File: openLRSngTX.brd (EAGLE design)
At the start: 50 x 40.2 mm, 28 parts, among them IC1 RFM23BPSMD, J1 AVR_SPI_PRG_6PTH, Q1 MMBT2222, U1 ATMEGA328P, X1 BU-SMA-V, Y1 16MHz

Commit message: minor updates
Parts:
- moved C6 4.50 mm to (36.8, 16.6), turned to 270 degrees
- moved C7 3.89 mm to (36.8, 20.2)
- moved C2 3.34 mm to (15.7, 33.5)
- moved C3 3.34 mm to (17.7, 33.5)
- moved S1 1.02 mm to (28.7, 20.1)
- moved C8 0.25 mm to (17.8, 11.9)
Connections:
- net TXD: now also JP1.4; no longer JP1.5
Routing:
- net N$15: track 0.00 -> 17.9 mm, vias 0 -> 2
- net GND: track 34.9 -> 29.3 mm, vias 7 -> 11
- net TXD: track 51.7 -> 49.9 mm
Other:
- board size 50 x 40.2 mm -> 50 x 40 mm

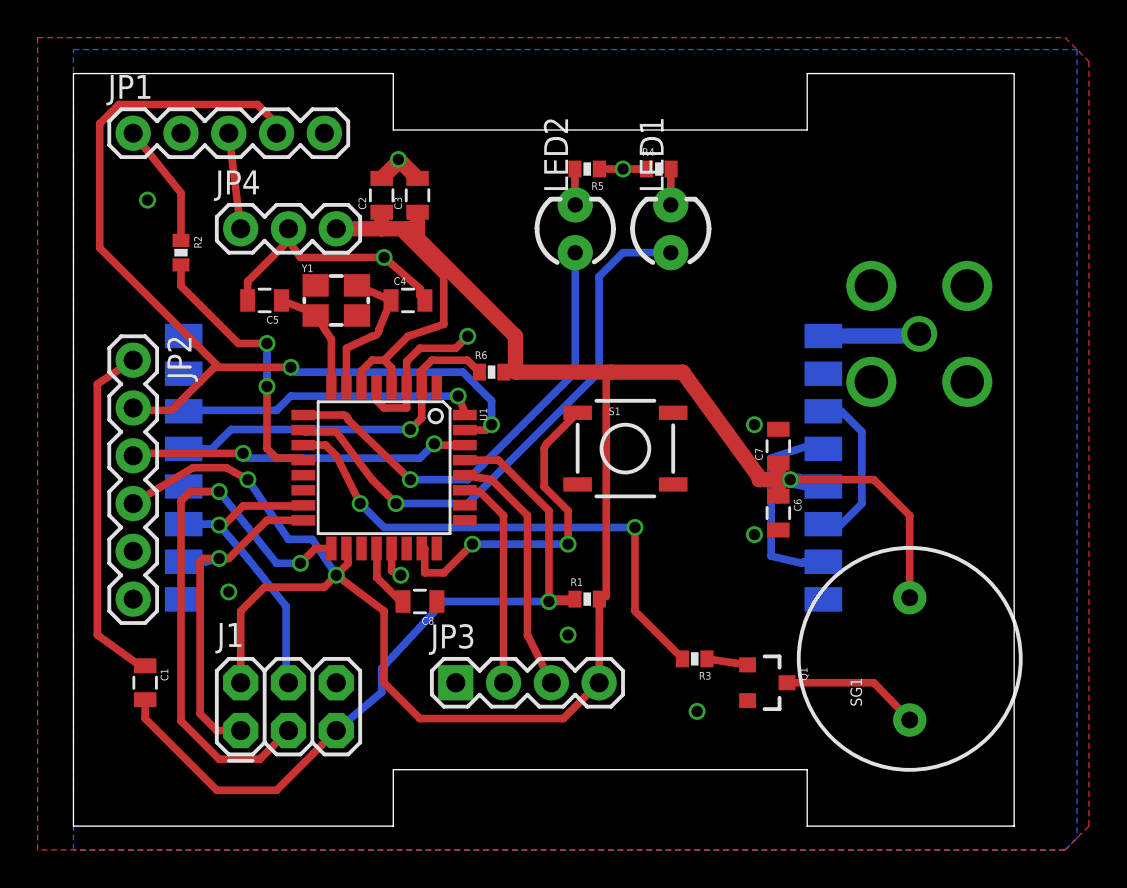
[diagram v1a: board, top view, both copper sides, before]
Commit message: Add resistor to TXD towards 'host' Add cutout over the antenna connection.
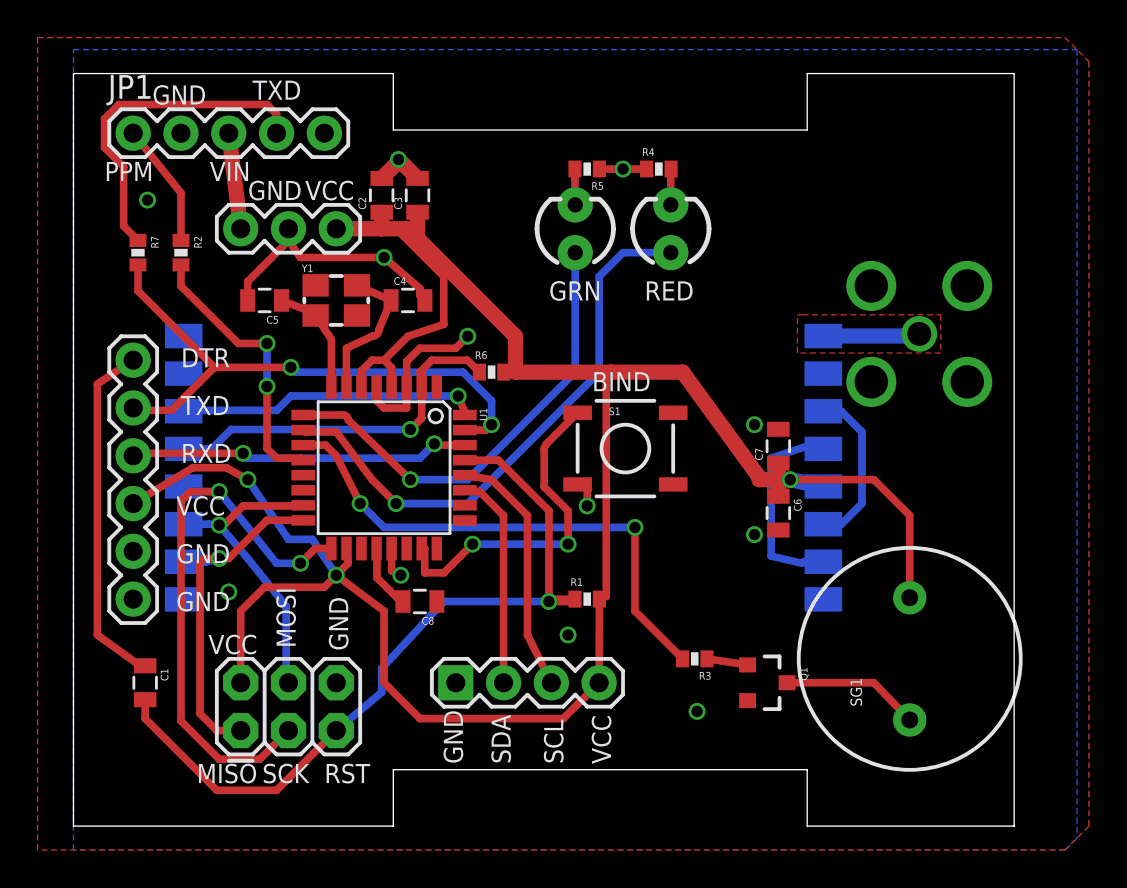
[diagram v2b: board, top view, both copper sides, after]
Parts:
- added R7: 1k, SparkFun-Resistors:0402-RES
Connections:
- new net N$17: JP1.4, R7.1
- net TXD: now also R7.2; no longer JP1.4
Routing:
- net TXD: track 49.9 -> 30.7 mm
- net N$17: track 0.00 -> 17.9 mm
- net GND: track 29.3 -> 31.0 mm, vias 11 -> 12
- added copper zone on layer 1, net N$16
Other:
- board text added: "BIND"
- board text added: "DTR"
- board text added: "GND"
- board text added: "GRN"
- board text added: "MISO"
- board text added: "MOSI"
- board text added: "PPM"
- board text added: "RED"
- board text added: "RST"
- board text added: "RXD"
- board text added: "SCK"
- board text added: "SCL"
- board text added: "SDA"
- board text added: "TXD"
- board text added: "VCC"
- board text added: "VIN"

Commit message: Small adjustments in board layout.
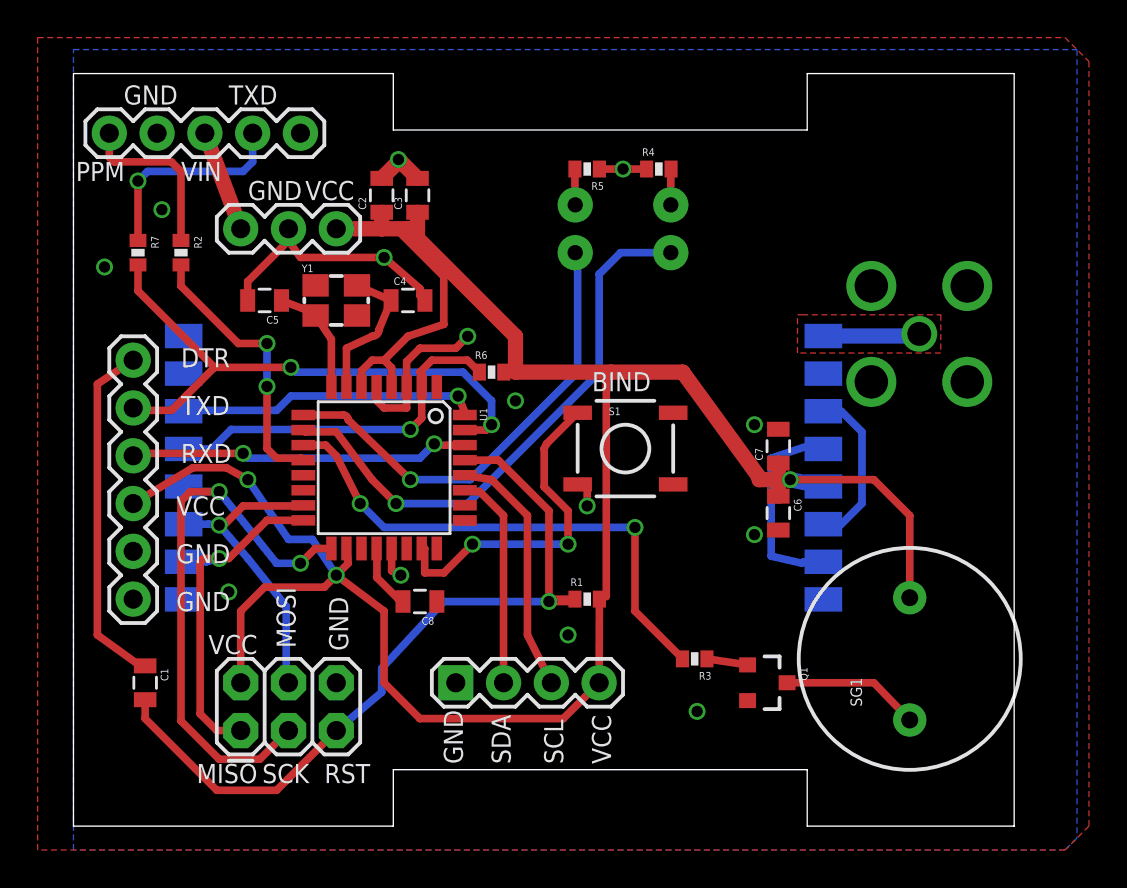
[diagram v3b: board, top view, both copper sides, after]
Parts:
- moved JP1 1.27 mm to (1.27, 36.8)
- flipped LED1 to the bottom
- flipped LED2 to the bottom
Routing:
- net N$17: track 17.9 -> 11.2 mm, vias 0 -> 1
- net N$3: track 6.59 -> 9.06 mm
- net N$10: vias 0 -> 1
- net GND: vias 12 -> 14
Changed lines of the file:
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@@
 <text x="5.08" y="21.844" size="1.016" layer="25">TXD</text>
 <text x="5.08" y="24.384" size="1.016" layer="25">DTR</text>
-<text x="1.016" y="34.29" size="1.016" layer="25">PPM</text>
-<text x="3.556" y="38.354" size="1.016" layer="25">GND</text>
-<text x="6.604" y="34.29" size="1.016" layer="25">VIN</text>
-<text x="8.89" y="38.608" size="1.016" layer="25">TXD</text>
+<text x="-0.508" y="34.29" size="1.016" layer="25">PPM</text>
+<text x="2.032" y="38.354" size="1.016" layer="25">GND</text>
+<text x="5.08" y="34.29" size="1.016" layer="25">VIN</text>
+<text x="7.62" y="38.354" size="1.016" layer="25">TXD</text>
 <text x="11.684" y="33.274" size="1.016" layer="25">VCC</text>
 <text x="8.636" y="33.274" size="1.016" layer="25">GND</text>
@@
 <text x="12.7" y="2.286" size="1.016" layer="25">RST</text>
 <text x="26.924" y="23.114" size="1.016" layer="25">BIND</text>
-<text x="24.638" y="27.94" size="1.016" layer="25">GRN</text>
-<text x="29.718" y="27.94" size="1.016" layer="25">RED</text>
+<text x="24.638" y="27.94" size="1.016" layer="26" rot="MR0">GRN</text>
+<text x="29.718" y="27.94" size="1.016" layer="26" rot="MR0">RED</text>
 </plain>
 <attributes>
@@
 <element name="R4" library="SparkFun-Resistors" package="0402-RES" value="220R" x="30.48" y="34.925"/>
 <element name="R5" library="SparkFun-Resistors" package="0402-RES" value="220R" x="26.67" y="34.925" rot="R180"/>
-<element name="LED1" library="SparkFun-LED" package="LED3MM" value="RED" x="31.115" y="31.75" smashed="yes" rot="R90"/>
-<element name="LED2" library="SparkFun-LED" package="LED3MM" value="GRN" x="26.035" y="31.75" smashed="yes" rot="R90"/>
+<element name="LED1" library="SparkFun-LED" package="LED3MM" value="RED" x="31.115" y="31.75" smashed="yes" rot="MR90"/>
+<element name="LED2" library="SparkFun-LED" package="LED3MM" value="GRN" x="26.035" y="31.75" smashed="yes" rot="MR90"/>
 <element name="SG1" library="SparkFun-Electromechanical" package="BUZZER-12MM" value="BUZZERPTH" x="43.815" y="8.89" smashed="yes" rot="R90">
 <attribute name="NAME" x="41.275" y="6.35" size="0.6096" layer="25" ratio="10" rot="R90"/>
@@
 </element>
 <element name="Y1" library="crystal_3225" package="CRYSTAL-SMD-5X3" value="16MHz" x="13.335" y="27.94"/>
-<element name="JP1" library="SparkFun-Connectors" package="1X05" value="IN" x="2.54" y="36.83" smashed="yes">
-<attribute name="NAME" x="1.1938" y="38.6588" size="1.27" layer="25" ratio="10"/>
-</element>
+<element name="JP1" library="SparkFun-Connectors" package="1X05" value="IN" x="1.27" y="36.83" smashed="yes"/>
 <element name="JP4" library="SparkFun-Connectors" package="1X03" value="REG" x="8.255" y="31.75" smashed="yes"/>
 <element name="C6" library="SparkFun-Capacitors" package="0805" value="1uF" x="36.83" y="16.637" rot="R270"/>
@@
 <via x="35.56" y="15.494" extent="1-16" drill="0.6"/>
 <via x="7.62" y="12.446" extent="1-16" drill="0.6"/>
-<via x="3.302" y="33.274" extent="1-16" drill="0.6"/>
+<via x="4.064" y="32.766" extent="1-16" drill="0.6"/>
 <via x="25.654" y="10.16" extent="1-16" drill="0.6"/>
 <via x="26.67" y="17.018" extent="1-16" drill="0.6"/>
 <wire x1="26.162" y1="18.161" x2="26.67" y2="18.161" width="0.4064" layer="1"/>
 <wire x1="26.67" y1="18.161" x2="26.67" y2="17.018" width="0.4064" layer="1"/>
+<via x="1.016" y="29.718" extent="1-16" drill="0.6"/>
+<via x="22.86" y="22.606" extent="1-16" drill="0.6"/>
 </signal>
 <signal name="VCC">
@@
 <contactref element="R2" pad="1"/>
 <contactref element="JP1" pad="1"/>
-<wire x1="5.08" y1="31.13" x2="5.08" y2="33.655" width="0.4064" layer="1"/>
-<wire x1="5.08" y1="33.655" x2="2.54" y2="36.83" width="0.4064" layer="1"/>
+<wire x1="5.08" y1="31.13" x2="5.08" y2="34.798" width="0.4064" layer="1"/>
+<wire x1="5.08" y1="34.798" x2="4.572" y2="35.306" width="0.4064" layer="1"/>
+<wire x1="4.572" y1="35.306" x2="1.524" y2="35.306" width="0.4064" layer="1"/>
+<wire x1="1.524" y1="35.306" x2="1.27" y2="35.56" width="0.4064" layer="1"/>
+<wire x1="1.27" y1="35.56" x2="1.27" y2="36.83" width="0.4064" layer="1"/>
 </signal>
 <signal name="N$4">
@@
 <contactref element="LED1" pad="A"/>
 <contactref element="U1" pad="10"/>
-<wire x1="31.115" y1="30.48" x2="28.575" y2="30.48" width="0.4064" layer="16"/>
-<wire x1="28.575" y1="30.48" x2="27.305" y2="29.21" width="0.4064" layer="16"/>
-<wire x1="27.305" y1="29.21" x2="27.305" y2="24.13" width="0.4064" layer="16"/>
+<wire x1="27.305" y1="29.337" x2="27.305" y2="24.13" width="0.4064" layer="16"/>
 <wire x1="27.305" y1="24.13" x2="20.32" y2="17.145" width="0.4064" layer="16"/>
 <wire x1="20.32" y1="17.145" x2="16.51" y2="17.145" width="0.4064" layer="16"/>
@@
 <wire x1="13.335" y1="20.955" x2="11.6774" y2="20.955" width="0.4064" layer="1"/>
 <wire x1="11.6774" y1="20.955" x2="11.5824" y2="21.05" width="0.4064" layer="1"/>
+<wire x1="27.305" y1="29.337" x2="28.448" y2="30.48" width="0.4064" layer="16"/>
+<wire x1="28.448" y1="30.48" x2="31.115" y2="30.48" width="0.4064" layer="16"/>
 </signal>
 <signal name="N$8">
@@
 <wire x1="13.97" y1="21.59" x2="17.272" y2="18.415" width="0.4064" layer="1"/>
 <via x="17.272" y="18.415" extent="1-16" drill="0.6"/>
-<wire x1="17.272" y1="18.415" x2="20.32" y2="18.415" width="0.4064" layer="16"/>
-<wire x1="20.32" y1="18.415" x2="26.035" y2="24.13" width="0.4064" layer="16"/>
-<wire x1="26.035" y1="24.13" x2="26.035" y2="30.48" width="0.4064" layer="16"/>
+<wire x1="17.272" y1="18.415" x2="20.447" y2="18.415" width="0.4064" layer="16"/>
+<wire x1="20.447" y1="18.415" x2="26.162" y2="24.13" width="0.4064" layer="16"/>
+<wire x1="26.162" y1="24.13" x2="26.162" y2="30.353" width="0.4064" layer="16"/>
+<wire x1="26.162" y1="30.353" x2="26.035" y2="30.48" width="0.4064" layer="16"/>
 </signal>
 <signal name="N$9">
@@
 <contactref element="R5" pad="2"/>
 <wire x1="26.02" y1="34.925" x2="26.02" y2="33.035" width="0.4064" layer="1"/>
-<wire x1="26.02" y1="33.035" x2="26.035" y2="33.02" width="0.4064" layer="1"/>
+<wire x1="26.02" y1="33.035" x2="26.035" y2="33.02" width="0.4064" layer="16"/>
+<via x="26.02" y="33.035" extent="1-16" drill="0.6"/>
 </signal>
 <signal name="N$11">
@@
 <contactref element="JP4" pad="1"/>
 <contactref element="JP1" pad="3"/>
-<wire x1="7.62" y1="36.83" x2="8.255" y2="31.75" width="0.8128" layer="1"/>
+<wire x1="6.35" y1="36.83" x2="8.255" y2="31.75" width="0.8128" layer="1"/>
 </signal>
 <signal name="N$24">
@@
 <contactref element="R7" pad="1"/>
 <contactref element="JP1" pad="4"/>
-<wire x1="10.16" y1="36.83" x2="10.16" y2="37.846" width="0.4064" layer="1"/>
-<wire x1="10.16" y1="37.846" x2="9.652" y2="38.354" width="0.4064" layer="1"/>
-<wire x1="9.652" y1="38.354" x2="1.778" y2="38.354" width="0.4064" layer="1"/>
-<wire x1="1.778" y1="38.354" x2="1.016" y2="37.592" width="0.4064" layer="1"/>
-<wire x1="1.016" y1="37.592" x2="1.016" y2="36.068" width="0.4064" layer="1"/>
-<wire x1="1.016" y1="36.068" x2="2.032" y2="35.052" width="0.4064" layer="1"/>
-<wire x1="2.032" y1="35.052" x2="2.032" y2="31.892" width="0.4064" layer="1"/>
-<wire x1="2.032" y1="31.892" x2="2.794" y2="31.13" width="0.4064" layer="1"/>
+<wire x1="8.89" y1="36.83" x2="8.89" y2="35.306" width="0.4064" layer="16"/>
+<wire x1="8.89" y1="35.306" x2="8.382" y2="34.798" width="0.4064" layer="16"/>
+<wire x1="8.382" y1="34.798" x2="3.302" y2="34.798" width="0.4064" layer="16"/>
+<wire x1="3.302" y1="34.798" x2="2.794" y2="34.29" width="0.4064" layer="16"/>
+<via x="2.794" y="34.29" extent="1-16" drill="0.6"/>
+<wire x1="2.794" y1="34.29" x2="2.794" y2="31.13" width="0.4064" layer="1"/>
 </signal>
 </signals>
